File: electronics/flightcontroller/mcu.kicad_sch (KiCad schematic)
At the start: 30 parts, among them J10 USB, J8 Micro_SD_Card_Det_HYC80-TF08-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, J9 SWD, SW1 RESET, U3 STM32G491CCUx, U6 GT-24-Mini, Y1 24MHz

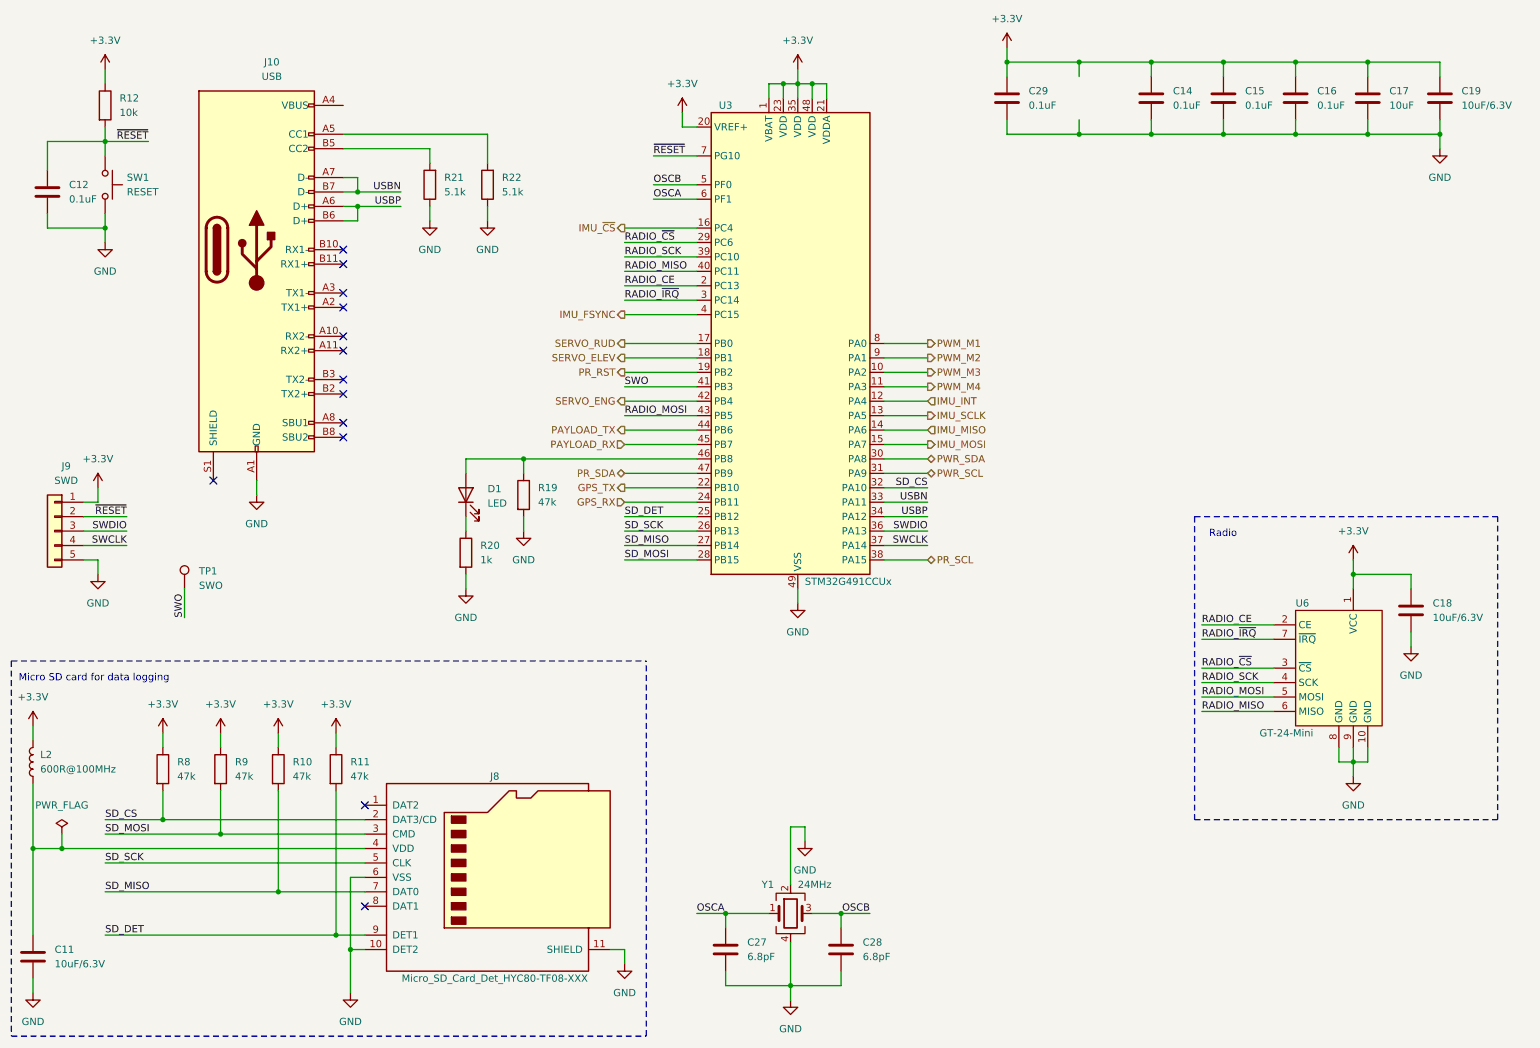
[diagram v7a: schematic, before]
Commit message: electronics: Add a resistor for ESC power and some test pads.
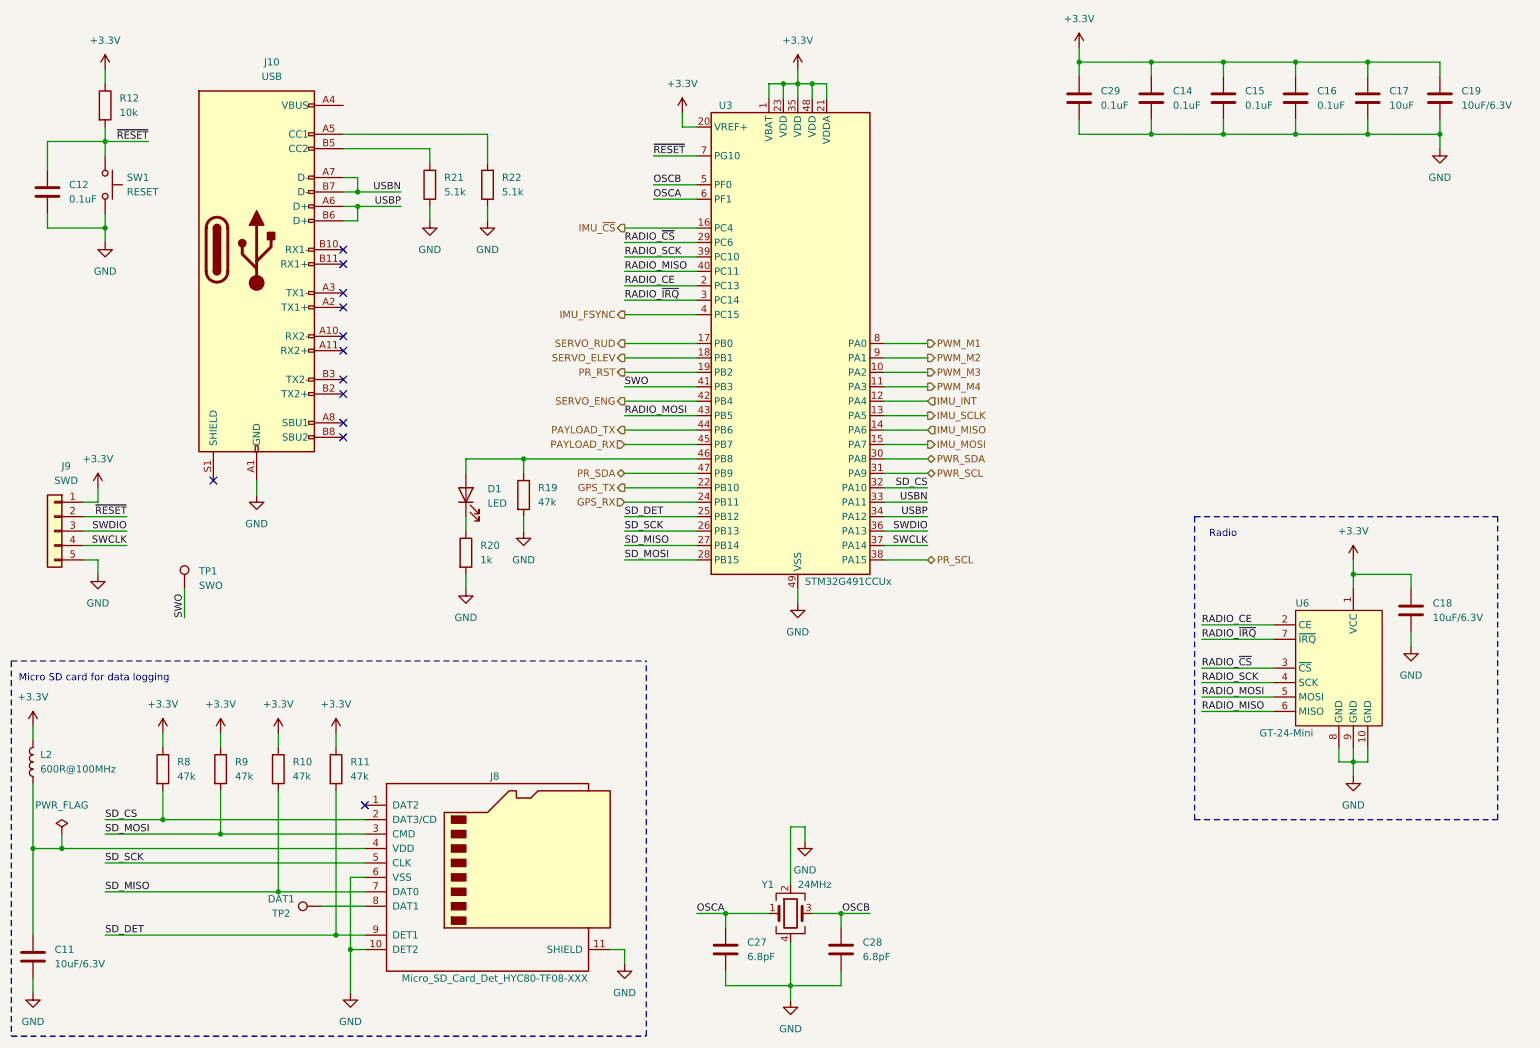
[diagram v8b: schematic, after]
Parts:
- added TP2: DAT1, TestPoint:TestPoint_Pad_D2.0mm, symbol Connector:TestPoint
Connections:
- net at J8.8 (DAT1): now also TP2.1
- no-connect marks 13 -> 12
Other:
- moved on the sheet: C29
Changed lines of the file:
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@@
   (junction (at 156.21 25.4) (diameter 0.9144) (color 0 0 0 0))
   (junction (at 161.29 171.45) (diameter 0.9144) (color 0 0 0 0))
-  (junction (at 190.5 21.59) (diameter 0.9144) (color 0 0 0 0))
   (junction (at 203.2 21.59) (diameter 0.9144) (color 0 0 0 0))
-  (junction (at 203.2 34.29) (diameter 0.9144) (color 0 0 0 0))
   (junction (at 215.9 21.59) (diameter 0.9144) (color 0 0 0 0))
   (junction (at 215.9 34.29) (diameter 0.9144) (color 0 0 0 0))
@@
   (no_connect (at 73.66 87.63))
   (no_connect (at 77.47 152.4))
-  (no_connect (at 77.47 170.18))
   (wire (pts (xy 19.05 138.43) (xy 19.05 140.97))
     (stroke (width 0) (type solid) (color 0 0 0 0))
@@
     (stroke (width 0) (type solid) (color 0 0 0 0))
   )
+  (wire (pts (xy 69.85 170.18) (xy 77.47 170.18))
+    (stroke (width 0) (type default) (color 0 0 0 0))
+  )
   (wire (pts (xy 72.39 139.7) (xy 72.39 142.24))
     (stroke (width 0) (type solid) (color 0 0 0 0))
@@
     (stroke (width 0) (type solid) (color 0 0 0 0))
   )
-  (wire (pts (xy 190.5 19.05) (xy 190.5 21.59))
-    (stroke (width 0) (type solid) (color 0 0 0 0))
-  )
-  (wire (pts (xy 190.5 21.59) (xy 190.5 24.13))
-    (stroke (width 0) (type solid) (color 0 0 0 0))
-  )
-  (wire (pts (xy 190.5 31.75) (xy 190.5 34.29))
-    (stroke (width 0) (type solid) (color 0 0 0 0))
-  )
-  (wire (pts (xy 190.5 34.29) (xy 203.2 34.29))
-    (stroke (width 0) (type solid) (color 0 0 0 0))
-  )
-  (wire (pts (xy 203.2 21.59) (xy 190.5 21.59))
+  (wire (pts (xy 203.2 19.05) (xy 203.2 21.59))
     (stroke (width 0) (type solid) (color 0 0 0 0))
   )
@@
     (stroke (width 0) (type solid) (color 0 0 0 0))
   )
+  (wire (pts (xy 203.2 21.59) (xy 215.9 21.59))
+    (stroke (width 0) (type solid) (color 0 0 0 0))
+  )
   (wire (pts (xy 203.2 31.75) (xy 203.2 34.29))
     (stroke (width 0) (type solid) (color 0 0 0 0))
   )
   (wire (pts (xy 203.2 34.29) (xy 215.9 34.29))
-    (stroke (width 0) (type solid) (color 0 0 0 0))
-  )
-  (wire (pts (xy 215.9 21.59) (xy 203.2 21.59))
     (stroke (width 0) (type solid) (color 0 0 0 0))
   )
@@
     (pin "1")
   )
-  (symbol (lib_id "power:+3.3V") (at 190.5 19.05 0) (unit 1)
-    (in_bom yes) (on_board yes) (fields_autoplaced)
-    (property "Reference" "#PWR0136" (id 0) (at 190.5 22.86 0)
-      (effects (font (size 1.27 1.27)) hide)
-    )
-    (property "Value" "+3.3V" (id 1) (at 190.5 13.97 0))
-    (property "Footprint" "" (id 2) (at 190.5 19.05 0)
-      (effects (font (size 1.27 1.27)) hide)
-    )
-    (property "Datasheet" "" (id 3) (at 190.5 19.05 0)
+  (symbol (lib_id "power:+3.3V") (at 203.2 19.05 0) (unit 1)
+    (in_bom yes) (on_board yes) (fields_autoplaced)
+    (property "Reference" "#PWR0136" (id 0) (at 203.2 22.86 0)
+      (effects (font (size 1.27 1.27)) hide)
+    )
+    (property "Value" "+3.3V" (id 1) (at 203.2 13.97 0))
+    (property "Footprint" "" (id 2) (at 203.2 19.05 0)
+      (effects (font (size 1.27 1.27)) hide)
+    )
+    (property "Datasheet" "" (id 3) (at 203.2 19.05 0)
       (effects (font (size 1.27 1.27)) hide)
     )
@@
     (pin "1")
   )
+  (symbol (lib_id "Connector:TestPoint") (at 69.85 170.18 90) (unit 1)
+    (in_bom yes) (on_board yes)
+    (property "Reference" "TP2" (id 0) (at 62.738 171.45 90))
+    (property "Value" "DAT1" (id 1) (at 62.738 168.91 90))
+    (property "Footprint" "TestPoint:TestPoint_Pad_D2.0mm" (id 2) (at 69.85 165.1 0)
+      (effects (font (size 1.27 1.27)) hide)
+    )
+    (property "Datasheet" "~" (id 3) (at 69.85 165.1 0)
+      (effects (font (size 1.27 1.27)) hide)
+    )
+    (pin "1")
+  )
   (symbol (lib_id "power:GND") (at 19.05 185.42 0) (unit 1)
     (in_bom yes) (on_board yes) (fields_autoplaced)
@@
     (pin "2")
   )
-  (symbol (lib_id "Device:C") (at 190.5 27.94 0) (unit 1)
-    (in_bom yes) (on_board yes) (fields_autoplaced)
-    (property "Reference" "C29" (id 0) (at 194.31 26.6699 0)
-      (effects (font (size 1.27 1.27)) (justify left))
-    )
-    (property "Value" "0.1uF" (id 1) (at 194.31 29.2099 0)
-      (effects (font (size 1.27 1.27)) (justify left))
-    )
-    (property "Footprint" "Capacitor_SMD:C_0402_1005Metric" (id 2) (at 191.4652 31.75 0)
-      (effects (font (size 1.27 1.27)) hide)
-    )
-    (property "Datasheet" "~" (id 3) (at 190.5 27.94 0)
-      (effects (font (size 1.27 1.27)) hide)
-    )
-    (property "Mouser" "81-GRM155R71H104KE4D" (id 4) (at 190.5 27.94 0)
+  (symbol (lib_id "Device:C") (at 203.2 27.94 0) (unit 1)
+    (in_bom yes) (on_board yes) (fields_autoplaced)
+    (property "Reference" "C29" (id 0) (at 207.01 26.6699 0)
+      (effects (font (size 1.27 1.27)) (justify left))
+    )
+    (property "Value" "0.1uF" (id 1) (at 207.01 29.2099 0)
+      (effects (font (size 1.27 1.27)) (justify left))
+    )
+    (property "Footprint" "Capacitor_SMD:C_0402_1005Metric" (id 2) (at 204.1652 31.75 0)
+      (effects (font (size 1.27 1.27)) hide)
+    )
+    (property "Datasheet" "~" (id 3) (at 203.2 27.94 0)
+      (effects (font (size 1.27 1.27)) hide)
+    )
+    (property "Mouser" "81-GRM155R71H104KE4D" (id 4) (at 203.2 27.94 0)
       (effects (font (size 1.27 1.27)) hide)
     )
@@
     (pin "1")
     (pin "2")
+  )
+  (symbol (lib_id "Device:Crystal_GND24") (at 152.4 171.45 0) (unit 1)
+    (in_bom yes) (on_board yes)
+    (property "Reference" "Y1" (id 0) (at 147.32 166.3699 0)
+      (effects (font (size 1.27 1.27)) (justify left))
+    )
+    (property "Value" "24MHz" (id 1) (at 153.67 166.3699 0)
+      (effects (font (size 1.27 1.27)) (justify left))
+    )
+    (property "Footprint" "Crystal:Crystal_SMD_2016-4Pin_2.0x1.6mm" (id 2) (at 152.4 171.45 0)
+      (effects (font (size 1.27 1.27)) hide)
+    )
+    (property "Datasheet" "~" (id 3) (at 152.4 171.45 0)
+      (effects (font (size 1.27 1.27)) hide)
+    )
+    (property "Digikey" "490-5575-1-ND" (id 4) (at 152.4 171.45 0)
+      (effects (font (size 1.27 1.27)) hide)
+    )
+    (property "Mouser" "81-XRCGB24M000F0L0R0" (id 5) (at 152.4 171.45 0)
+      (effects (font (size 1.27 1.27)) hide)
+    )
+    (pin "1")
+    (pin "2")
+    (pin "3")
+    (pin "4")
   )
   (symbol (lib_id "Connector_Generic:Conn_01x05") (at 22.86 104.14 0) (mirror y) (unit 1)
@@
     (pin "5")
   )
-  (symbol (lib_id "Device:Crystal_GND24") (at 152.4 171.45 0) (unit 1)
-    (in_bom yes) (on_board yes)
-    (property "Reference" "Y1" (id 0) (at 147.32 166.3699 0)
-      (effects (font (size 1.27 1.27)) (justify left))
-    )
-    (property "Value" "24MHz" (id 1) (at 153.67 166.3699 0)
-      (effects (font (size 1.27 1.27)) (justify left))
-    )
-    (property "Footprint" "Crystal:Crystal_SMD_2016-4Pin_2.0x1.6mm" (id 2) (at 152.4 171.45 0)
-      (effects (font (size 1.27 1.27)) hide)
-    )
-    (property "Datasheet" "~" (id 3) (at 152.4 171.45 0)
-      (effects (font (size 1.27 1.27)) hide)
-    )
-    (property "Digikey" "490-5575-1-ND" (id 4) (at 152.4 171.45 0)
-      (effects (font (size 1.27 1.27)) hide)
-    )
-    (property "Mouser" "81-XRCGB24M000F0L0R0" (id 5) (at 152.4 171.45 0)
-      (effects (font (size 1.27 1.27)) hide)
-    )
-    (pin "1")
-    (pin "2")
-    (pin "3")
-    (pin "4")
-  )
   (symbol (lib_id "flightcontroller-symbols:GT-24-Mini") (at 248.92 128.27 0) (unit 1)
